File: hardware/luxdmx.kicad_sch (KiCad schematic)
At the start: 93 parts, among them J1 XLR-5 NC5FAH, J2 USB-C, J3 HY931147C, J4 DISP SH9, J5 XLR-5 NC5FAH, J6 EXP SH9, J7 DMX-OUT A, J8 DMX-OUT B, Q1 MMBT3904, Q2 MMBT3904, SW1 BOOT, SW2 RST, U1 ESP32-S3-WROOM-1-N8, U2 W5500, U3 CH340C, U4 SY8089, U5 ISO3086DWR, U6 ISO3086DWR, U7 DP9900M-5V, U8 USBLC6-2SC6, U9 TPS2116DRLR, Y1 25MHz

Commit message: hw: LuxDMX v5, DMX512-A Protected outputs + reproducible route/validate pipeline (#60)
## What this is

v5 of the board. The headline: the DMX outputs are now DMX512-A "Protected" (E1.11 Annex C). A series Bourns TBU high-speed protector on each data pin survives a sustained fault, someone plugging mains (~30 VAC) or up to +-42 VDC into the XLR, and the board self-recovers when it's pulled. SPICE-confirmed clamp. Board grew 20mm on the right so the TBU gets its 4mm creepage barrier and all four corner mounting holes stay on GND (no EMC compromise, no NC'd holes).

On top of that the board finally has a reproducible routing + validation pipeline, so a re-spin isn't a manual afternoon anymore.

## Hardware
- Series TBU-CA065-200-WH per DMX data line. Fault-protected outputs per E1.11 Annex C, full breakdown in `hardware/E1.11_COMPLIANCE.md`.
- Board widened for the TBU creepage; corner mounting holes kept on GND.
- Post-validation hardening: via annular tightened (0.13mm min ring), fine-pitch clearance, stackup, silk reference-designator cleanup.

## Reproducible pipeline (two commands)
- `bash route_all.sh` sets net classes (Default 0.20 / Power 0.40 / Fine 0.15mm, Fine only on the W5500-dense nets), rebuilds planes + stitch vias, escapes the connectors, runs Freerouting, finishes any partials + a maze straggler, cleans pads, tightens the PoE void, widens the eth pairs. Hands-off.
- `bash validate_all.sh` runs 7 gates: connectivity (0 unrouted, DRC-enforced), DRC, geometry/DFM + current, DMX isolation, electrical, EMC placement, and critical-net signal integrity (eth/SPI/crystal length, vias, intra-pair skew, detour, net-class widths). All 7 hard gates pass.

## Fab
Gerbers, CPL and the JLCPCB BOM regenerated, all hard-gated on 0 unrouted.

## Honest caveats
Still a first-spin prototype, never been fabricated. The Ethernet MDI pairs are widened toward ~50 ohm single-ended but they are not controlled-impedance and not length-matched or coupled (that stays a supervised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
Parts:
- added F2, F3, F4, F5: TBU 200mA 650V, C913221:DIO-SMD_3P-L6.5-W4.0-BI, symbol luxdmx:TBU-CA065-200-WH
- added R20, R21, R22, R23: 470R, Resistor_SMD:R_0402_1005Metric, symbol luxdmx:R__v
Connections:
- net DMX2_A: now also R22.1
- net DMX2_AO: now also F4.3 (OUT/IN); no longer J5.3 (DATA+), J8.3
- net DMX2_B: now also R23.1
- net DMX2_BO: now also F5.3 (OUT/IN); no longer J5.2 (DATA-), J8.2
- net DMX_A: now also R20.1
- net DMX_AO: now also F2.3 (OUT/IN); no longer J1.3 (DATA+), J7.3
- net DMX_B: now also R21.1
- net DMX_BO: now also F3.3 (OUT/IN); no longer J1.2 (DATA-), J7.2
- net GNDISO: now also R21.2
- net GNDISO2: now also R23.2
- net VISO2_DRV: now also R22.2
- net VISO_DRV: now also R20.2
- new net DMX2_AX: F4.1 (IN/OUT), J5.3 (DATA+), J8.3
- new net DMX2_BX: F5.1 (IN/OUT), J5.2 (DATA-), J8.2
- new net DMX_AX: F2.1 (IN/OUT), J1.3 (DATA+), J7.3
- new net DMX_BX: F3.1 (IN/OUT), J1.2 (DATA-), J7.2
- no-connect marks 37 -> 41
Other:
- note added: "Misc"
- title: LuxDMX v4 - Art-Net/sACN -> isolated DMX gateway -> LuxDMX v5.00 - Art-Net/sACN -> isolated DMX gateway

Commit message: hw: v5.2 -- native USB, TPS2116 priority mode, 3225 crystal
Fixes the two hardware defects the v5.00 first article turned up, and drops the
serial bridge while we're in there. Revision goes to v5.2.

The auto-reset transistors had EN and IO0 on the wrong collectors, so flashing
needed the manual BOOT-button dance and a tool asserting DTR or RTS alone could
yank either line. Rather than swap the collectors, the whole bridge is gone:
U3, Q1, Q2, R6, R7 and C15 removed. USB-C now goes straight to the S3's native
USB-Serial-JTAG on IO19/IO20, which is in ROM and gives us the flashing port,
the console and JTAG for free. esptool resets over USB by itself, so there is
no auto-reset circuit left to mis-wire. Six parts fewer, two fewer part numbers
to source, and UART0 is free now (broken out on J6 pins 8/9).

The PoE to USB handover hung the board. The suspected cause (too little cap on
the USB input) was wrong: MODE and PR1 were tied to GND, which selects the
TPS2116's default "higher voltage wins" mode, and two near-equal 5V sources
make that hunt. It runs in priority mode now, MODE on VIN1 so PoE always wins,
with a 30k/10k PR1 divider putting the switchover at 4.0V. Vsw is high on
purpose: VOUT tracks VIN1 down until the switch actually fires, so 4.0V keeps
the rail well clear of the ~2.8V where the ESP hangs.

Crystal moved from the 2520 to the 3225 package (C9006, CL 12pF, so 18pF C0G
load caps). The 2520 kept going out of stock at JLC, the 3225 is the mainstream
size that is always there. R24 also went to a 714k-stock SKU.

Board is fully routed: 0 unrouted, 0 hard DRC. The schematic was stale (it
still had the CH340), so it is regenerated from the netlist and round-trip
verified against it, 0 diff on real nets. BOM/CPL/gerbers regenerated, all 93
parts sourced against live JLC assembly stock (not LCSC retail, which is a
different pool and had me chasing a phantom shortage).

None of this is validated on hardware. No physical board carries any of these
fixes yet.
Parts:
- removed C15: 100nF, Capacitor_SMD:C_0402_1005Metric, symbol luxdmx:C__v
- removed Q1, Q2: MMBT3904, Package_TO_SOT_SMD:SOT-23, symbol luxdmx:MMBT3904
- removed R6, R7: 10k, Resistor_SMD:R_0402_1005Metric, symbol luxdmx:R
- removed U3: CH340C, C84681:SOP-16_L10.0-W3.9-P1.27-LS6.0-BL, symbol luxdmx:CH340C
- added R24: 30k, Resistor_SMD:R_0402_1005Metric, symbol luxdmx:R__v
- added R25: 10k, Resistor_SMD:R_0402_1005Metric, symbol luxdmx:R__v
- C12, C13: value 33pF C0G -> 18pF C0G
- R9: symbol luxdmx:R__v -> luxdmx:R
- Y1: footprint Crystal:Crystal_SMD_2520-4Pin_2.5x2.0mm -> Crystal:Crystal_SMD_3225-4Pin_3.2x2.5mm
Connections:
- net +5V_POE: now also U9.3 (VIN1), U9.5 (MODE), R24.1; no longer U9.6 (VIN2)
- net +5V_USBF: now also U9.6 (VIN2); no longer U9.3 (VIN1)
- net GND: now also R25.2; no longer U9.4 (PR1), U9.5 (MODE)
- net S3_RX: now also J6.9
- net S3_TX: now also J6.8
- net USB_DM: now also U1.13 (IO19)
- net USB_DP: now also U1.14 (IO20)
- removed net EXP_IO19: J6.8, U1.13 (IO19)
- removed net EXP_IO20: J6.9, U1.14 (IO20)
- new net N$4: R24.2, R25.1, U9.4 (PR1)
- no-connect marks 41 -> 34
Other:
- note added: "PoE PD (U7) + 5V priority mux (U9 TPS2116, PoE preferred)"
- note added: "USB-C (J2) + ESD (U8) -> S3 native USB (USB-Serial-JTAG on IO19/IO20)"
- note removed: "PoE PD (U7) + 5V ideal-diode OR-ing (U9 TPS2116)"
- note removed: "U3 CH340 USB-UART + USB-C (J2) + auto-reset"
- moved on the sheet: C10, C11, C12, C13, C14, C16, C17, C18, C19, C20, C21, C22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

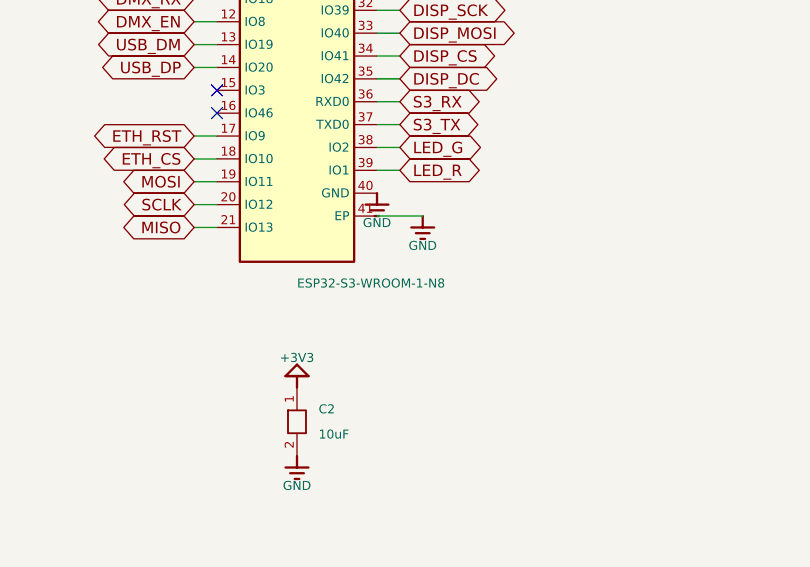
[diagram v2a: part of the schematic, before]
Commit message: hw: ESP32-S3-WROOM-1-N8R2 (+2MB PSRAM), and un-hardcode the pipeline paths
Module goes from the N8 to the **N8R2** (C2913204): same 8MB flash, plus 2MB
PSRAM. Same module, same footprint, same pinout, so this is a pure part swap
with no netlist rewiring and no re-route.

The thing worth writing down: the N8R2's PSRAM is QUAD, and quad does not touch
GPIO33-37. Only the OCTAL parts (R8 and up) wire those to the memory. Our
IO35/36/37 carry EXP_IO35/36/37 on the expansion header, so they survive the
swap untouched. Espressif: "When using Octal flash or Octal PSRAM or both,
GPIO33 ~ GPIO37 are connected to SPIIO4 ~ SPIIO7 and SPIDQS, and therefore on
boards embedded with ESP32-S3R8 / ESP32-S3R8V chip, GPIO33 ~ GPIO37 are not
recommended for other uses."

That also fixes a wrong claim in the README, which said the N8 "frees up
GPIO33-37, which we need for the LEDs + display". The LEDs and display are
nowhere near those pins; 35/36/37 go to the expansion header.

Second thing, and this one bit me while doing the swap: gen_bom_from_board.py
and four of the validate_* gates had the board path HARDCODED to
C:\dev\DMX\hardware. Run from anywhere else (a worktree, a second checkout)
they silently read and write the OTHER tree. gen_bom quietly rewrote the main
checkout's BOM while leaving the one next to it untouched, and worse,
validate_placement is wired into gen_gerbers, so the export's placement gate was
checking a different board than the one being exported. All five are HERE-relative
now, like gen_gerbers and gen_schematic already were.

Schematic regenerated and round-trip verified against the netlist again: 0 diff
on real nets. BOM regenerated. Gerbers untouched on purpose, the module's value
text lives on F.Fab and F.Fab is not in the gerber package.
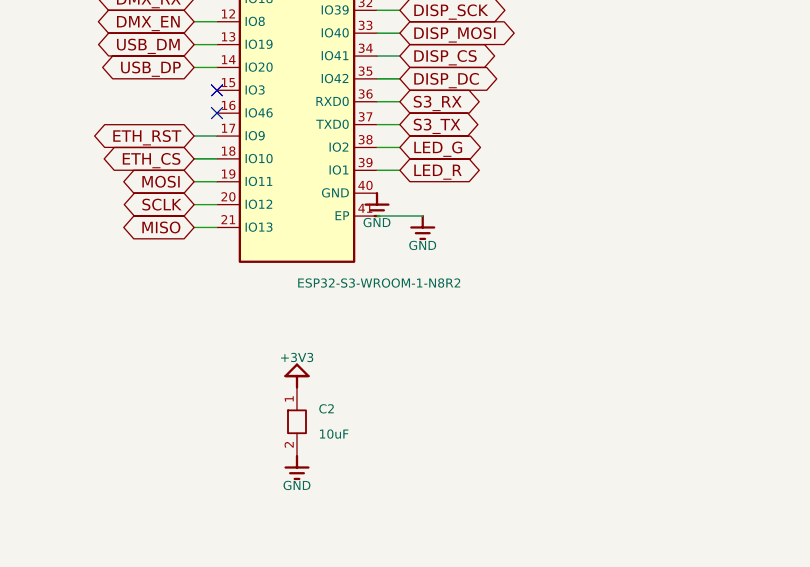
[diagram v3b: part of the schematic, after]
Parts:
- U1: value ESP32-S3-WROOM-1-N8 -> ESP32-S3-WROOM-1-N8R2; symbol luxdmx:ESP32-S3-WROOM-1-N8 -> luxdmx:ESP32-S3-WROOM-1-N8R2
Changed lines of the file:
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@@
 	(title_block (title "LuxDMX v5.00 - Art-Net/sACN -> isolated DMX gateway") (rev "v5.00") (comment 1 "auto-generated from luxdmx.net by gen_schematic.py"))
 	(text "U1  ESP32-S3-WROOM-1  +  reset / boot" (exclude_from_sim no) (at 12.7 28.4 0) (effects (font (size 2.2 2.2) (bold yes)) (justify left bottom)))
-	(symbol (lib_id "luxdmx:ESP32-S3-WROOM-1-N8") (at 132.08 85.09 0) (unit 1) (exclude_from_sim no) (in_bom yes) (on_board yes) (dnp no)
+	(symbol (lib_id "luxdmx:ESP32-S3-WROOM-1-N8R2") (at 132.08 85.09 0) (unit 1) (exclude_from_sim no) (in_bom yes) (on_board yes) (dnp no)
 		(property "Reference" "U1" (at 132.08 54.28 0) (effects (font (size 1 1)) (justify left)))
-		(property "Value" "ESP32-S3-WROOM-1-N8" (at 132.08 116.7 0) (effects (font (size 1 1)) (justify left)))
+		(property "Value" "ESP32-S3-WROOM-1-N8R2" (at 132.08 116.7 0) (effects (font (size 1 1)) (justify left)))
 		(property "Footprint" "RF_Module:ESP32-S3-WROOM-1" (at 132.08 85.09 0) (effects (font (size 0.8 0.8)) (hide yes)))
 		(property "Datasheet" "" (at 132.08 85.09 0) (effects (font (size 1.27 1.27)) (hide yes)))
